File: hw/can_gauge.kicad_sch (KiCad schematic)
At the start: 27 parts, among them J1 Gauge 1, J2 Gauge 2, J3 Gauge 3, J4 Gauge 4, J5 Gauge 5, J6 Power and CAN, U1 PIC16F1459-ISS, U2 MCP2515-xST, U3 MCP2561T-E/SN, U4 74HC595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

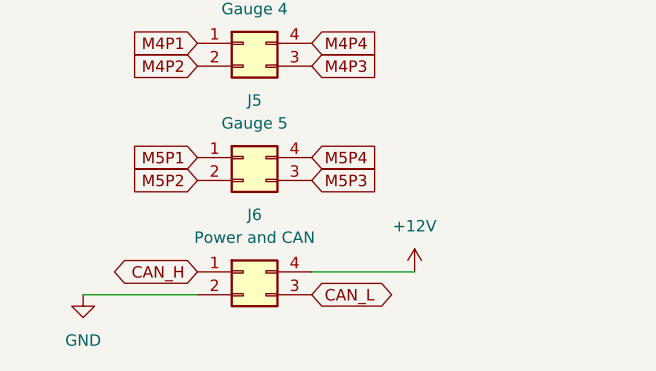
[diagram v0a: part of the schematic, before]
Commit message: hw: change connector layout
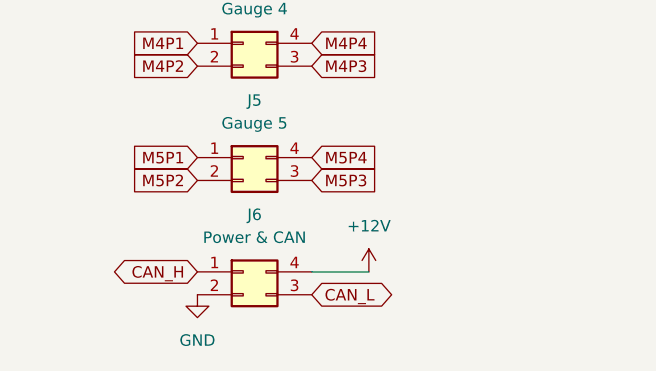
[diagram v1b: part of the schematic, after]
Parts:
- J6: value Power and CAN -> Power & CAN
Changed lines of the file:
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@@
 	(wire
 		(pts
+			(xy 58.42 262.89) (xy 64.77 262.89)
+		)
+		(stroke
+			(width 0)
+			(type default)
+		)
+	)
+	(wire
+		(pts
 			(xy 248.92 123.19) (xy 248.92 186.69)
 		)
@@
 	(wire
 		(pts
-			(xy 58.42 262.89) (xy 69.85 262.89)
-		)
-		(stroke
-			(width 0)
-			(type default)
-		)
-	)
-	(wire
-		(pts
 			(xy 224.79 54.61) (xy 257.81 54.61)
 		)
@@
 	(wire
 		(pts
-			(xy 33.02 265.43) (xy 45.72 265.43)
-		)
-		(stroke
-			(width 0)
-			(type default)
-		)
-	)
-	(wire
-		(pts
 			(xy 341.63 110.49) (xy 344.17 110.49)
 		)
@@
 		(lib_name "GND_5")
 		(lib_id "power:GND")
-		(at 33.02 265.43 0)
+		(at 45.72 265.43 0)
 		(unit 1)
 		(exclude_from_sim no)
@@
 		(fields_autoplaced yes)
 		(property "Reference" "#PWR09"
-			(at 33.02 271.78 0)
+			(at 45.72 271.78 0)
 			(effects
 				(font
@@
 		)
 		(property "Value" "GND"
-			(at 33.02 270.51 0)
+			(at 45.72 270.51 0)
 			(effects
 				(font
@@
 		)
 		(property "Footprint" ""
-			(at 33.02 265.43 0)
+			(at 45.72 265.43 0)
 			(effects
 				(font
@@
 		)
 		(property "Datasheet" ""
-			(at 33.02 265.43 0)
+			(at 45.72 265.43 0)
 			(effects
 				(font
@@
 		)
 		(property "Description" "Power symbol creates a global label with name \"GND\" , ground"
-			(at 33.02 265.43 0)
+			(at 45.72 265.43 0)
 			(effects
 				(font
@@
 		(lib_name "+12V_1")
 		(lib_id "power:+12V")
-		(at 69.85 262.89 0)
+		(at 64.77 262.89 0)
 		(unit 1)
 		(exclude_from_sim no)
@@
 		(fields_autoplaced yes)
 		(property "Reference" "#PWR08"
-			(at 69.85 266.7 0)
+			(at 64.77 266.7 0)
 			(effects
 				(font
@@
 		)
 		(property "Value" "+12V"
-			(at 69.85 257.81 0)
+			(at 64.77 257.81 0)
 			(effects
 				(font
@@
 		)
 		(property "Footprint" ""
-			(at 69.85 262.89 0)
+			(at 64.77 262.89 0)
 			(effects
 				(font
@@
 		)
 		(property "Datasheet" ""
-			(at 69.85 262.89 0)
+			(at 64.77 262.89 0)
 			(effects
 				(font
@@
 		)
 		(property "Description" "Power symbol creates a global label with name \"+12V\""
-			(at 69.85 262.89 0)
+			(at 64.77 262.89 0)
 			(effects
 				(font
@@
 			)
 		)
-		(property "Value" "Power and CAN"
+		(property "Value" "Power & CAN"
 			(at 52.07 259.08 0)
 			(effects

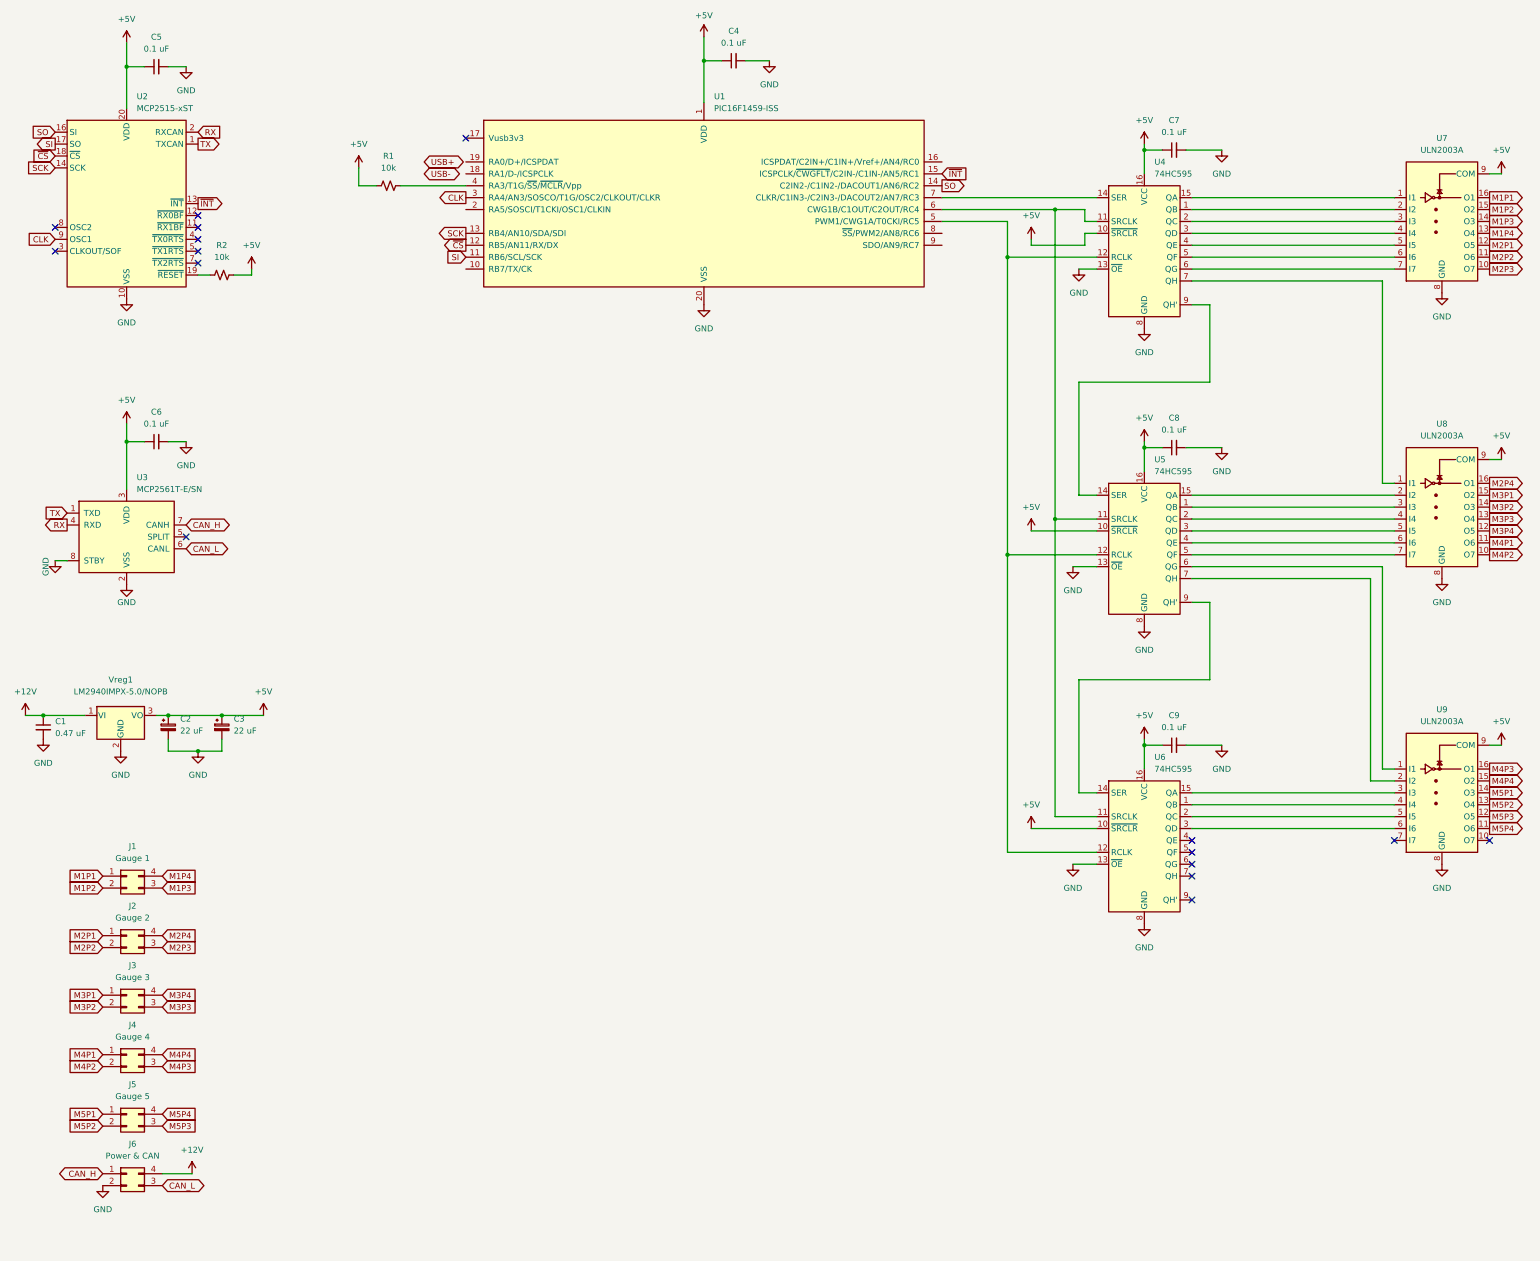
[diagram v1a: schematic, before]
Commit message: hw: 8-way transistor arrays, 6 gauges
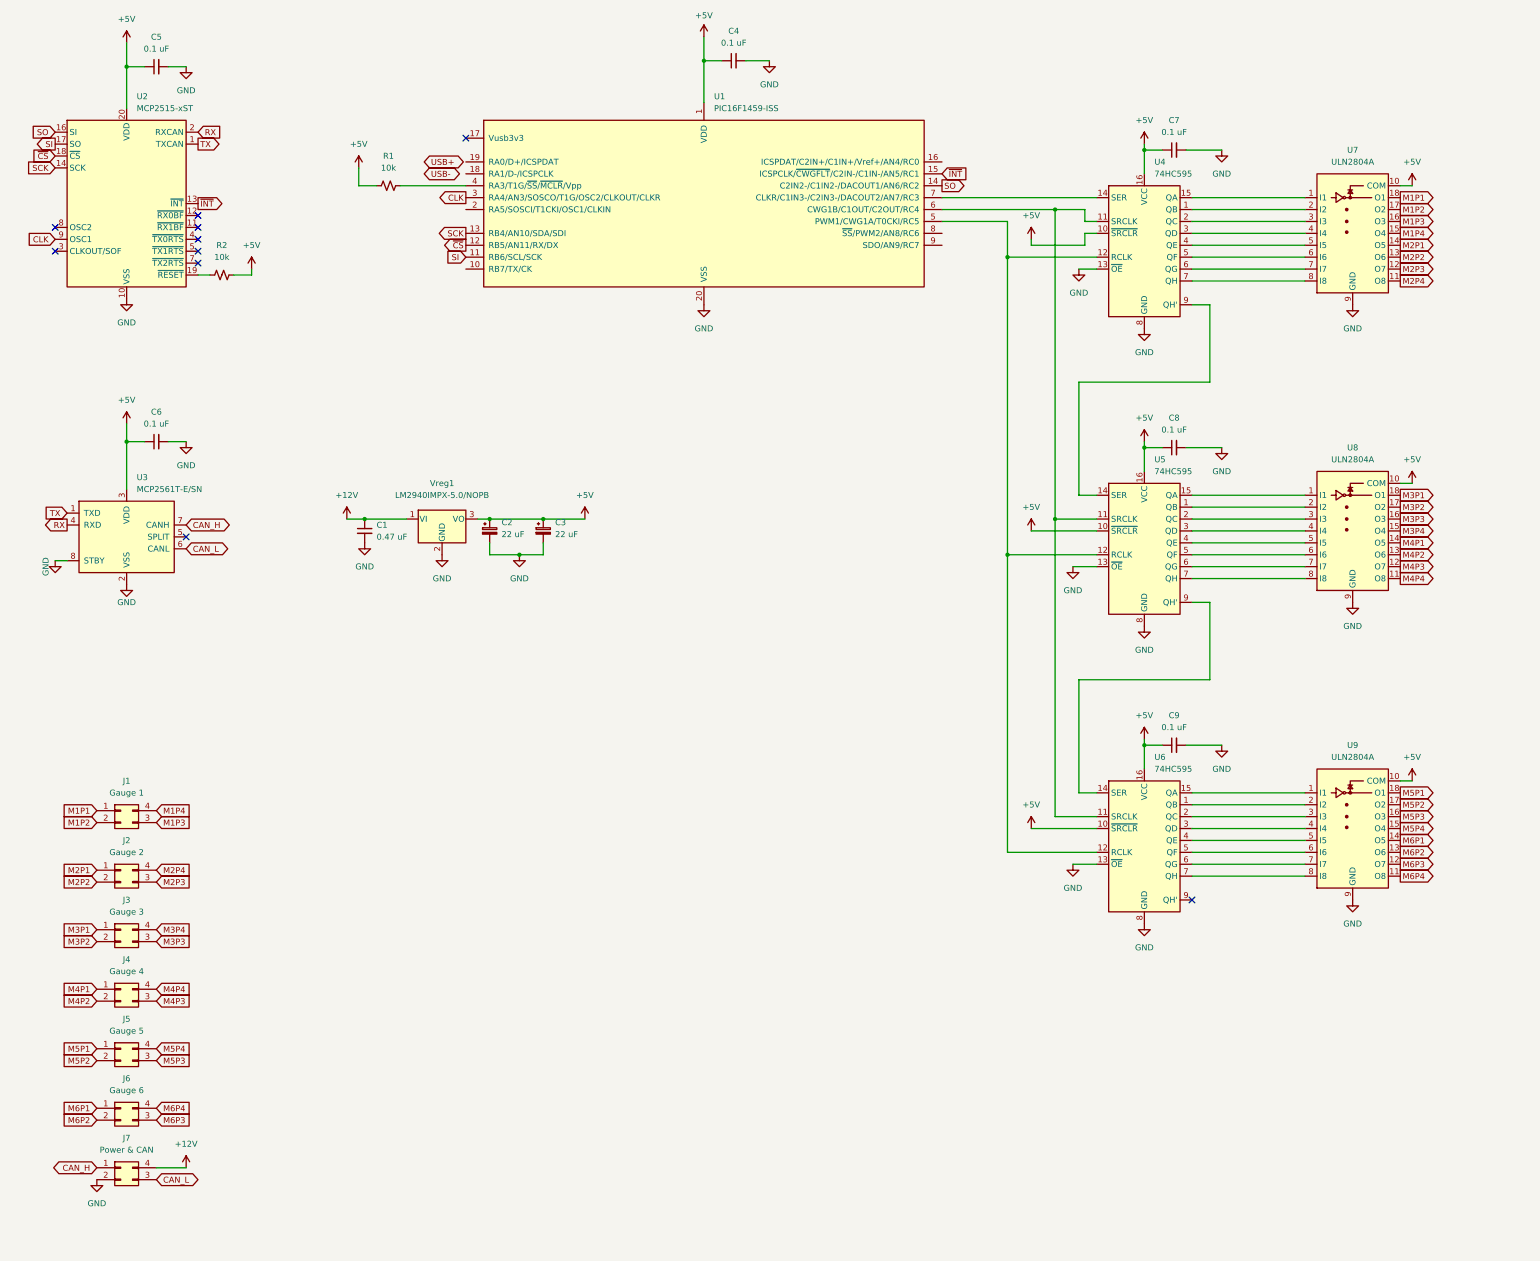
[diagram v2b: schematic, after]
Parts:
- removed U7, U8, U9: ULN2003A, Package_SO:SO-16_3.9x9.9mm_P1.27mm, symbol Transistor_Array:ULN2003A
- added J6: Gauge 6, Connector_Molex:Molex_Mini-Fit_Jr_5569-04A2_2x02_P4.20mm_Horizontal, symbol Connector_Generic:Conn_02x02_Counter_Clockwise
- added U7, U8, U9: ULN2804A, Package_DIP:DIP-18_W7.62mm, symbol Transistor_Array:ULN2804A
- U4, U5, U6: footprint Package_SO:TSSOP-16_4.4x5mm_P0.65mm -> Package_SO:SOIC-16W_7.5x10.3mm_P1.27mm; Digikey (none) -> https://www.digikey.ca/en/products/detail/texas-instruments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
- renumbered J6 to J7
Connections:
- net +5V: now also U7.10 (COM), U8.10 (COM), U9.10 (COM)
- net GND: now also U7.9 (GND), U8.9 (GND), U9.9 (GND)
- net M1P1: now also U7.18 (O1)
- net M1P2: now also U7.17 (O2)
- net M1P3: now also U7.16 (O3)
- net M1P4: now also U7.15 (O4)
- net M2P1: now also U7.14 (O5)
- net M2P2: now also U7.13 (O6)
- net M2P3: now also U7.12 (O7)
- net M2P4: now also U7.11 (O8)
- net M3P1: now also U8.18 (O1)
- net M3P2: now also U8.17 (O2)
- net M3P3: now also U8.16 (O3)
- net M3P4: now also U8.15 (O4)
- net M4P1: now also U8.14 (O5)
- net M4P2: now also U8.13 (O6)
- net M4P3: now also U8.12 (O7)
- net M4P4: now also U8.11 (O8)
- net M5P1: now also U9.18 (O1)
- net M5P2: now also U9.17 (O2)
- net M5P3: now also U9.16 (O3)
- net M5P4: now also U9.15 (O4)
- net at U5.1 (QB): now also U8.2 (I2)
- net at U5.15 (QA): now also U8.1 (I1)
- net at U5.2 (QC): now also U8.3 (I3)
- net at U5.3 (QD): now also U8.4 (I4)
- net at U5.4 (QE): now also U8.5 (I5)
- net at U5.5 (QF): now also U8.6 (I6)
- net at U5.6 (QG): now also U8.7 (I7)
- net at U5.7 (QH): now also U8.8 (I8)
- net at U4.7 (QH): now also U7.8 (I8)
- net at U4.15 (QA): now also U7.1 (I1)
- net at U4.1 (QB): now also U7.2 (I2)
- net at U4.2 (QC): now also U7.3 (I3)
- net at U4.3 (QD): now also U7.4 (I4)
- net at U4.4 (QE): now also U7.5 (I5)
- net at U4.5 (QF): now also U7.6 (I6)
- net at U4.6 (QG): now also U7.7 (I7)
- net at U6.15 (QA): now also U9.1 (I1)
- net at U6.1 (QB): now also U9.2 (I2)
- net at U6.2 (QC): now also U9.3 (I3)
- net at U6.3 (QD): now also U9.4 (I4)
- net at U6.4 (QE): now also U9.5 (I5)
- net at U6.5 (QF): now also U9.6 (I6)
- net at U6.6 (QG): now also U9.7 (I7)
- net at U6.7 (QH): now also U9.8 (I8)
- new net M6P1: J6.1 (Pin_1), U9.14 (O5)
- new net M6P2: J6.2 (Pin_2), U9.13 (O6)
- new net M6P3: J6.3 (Pin_3), U9.12 (O7)
- new net M6P4: J6.4 (Pin_4), U9.11 (O8)
- no-connect marks 16 -> 10
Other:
- moved on the sheet: C1, C2, C3, J1, J2, J3, J4, J5, J7, Vreg1

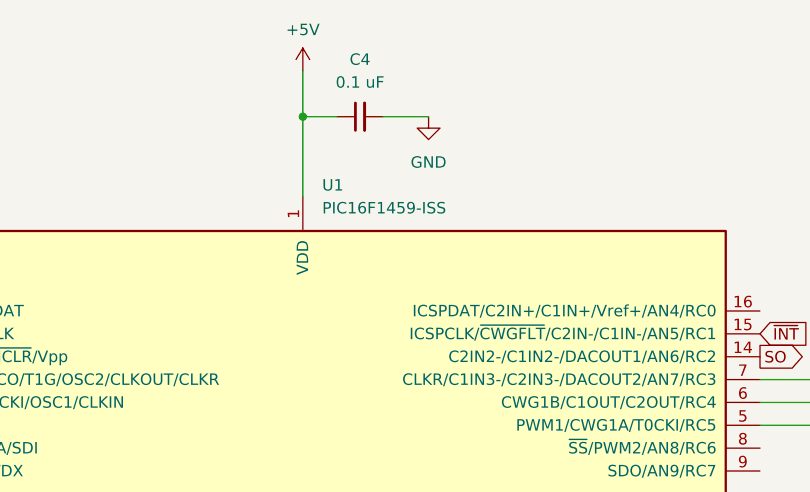
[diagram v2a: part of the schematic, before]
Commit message: hw: through-hole shift registers
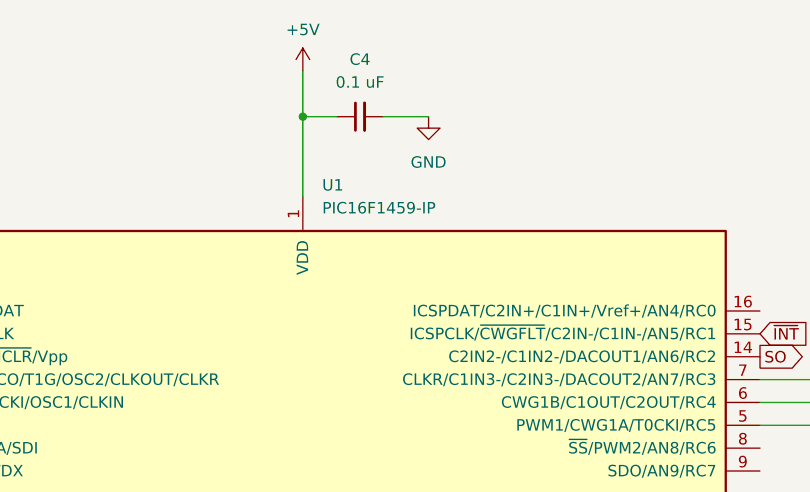
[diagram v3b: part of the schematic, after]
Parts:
- removed U1: PIC16F1459-ISS, Package_SO:SSOP-20_5.3x7.2mm_P0.65mm, symbol MCU_Microchip_PIC16:PIC16F1459-ISS
- added U1: PIC16F1459-IP, Package_DIP:DIP-20_W7.62mm, symbol MCU_Microchip_PIC16:PIC16F1459-IP
- C4, C5, C6, C7, C8, C9: footprint Capacitor_SMD:C_0402_1005Metric -> Capacitor_THT:C_Rect_L4.0mm_W2.5mm_P2.50mm; Digikey https://www.digikey.ca/en/products/detail/murata-electronic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 -> https://www.digikey.ca/en/products/detail/tdk-corporation/F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
- U4, U5, U6: footprint Package_SO:SOIC-16W_7.5x10.3mm_P1.27mm -> Package_DIP:DIP-16_W7.62mm; Digikey https://www.digikey.ca/en/products/detail/texas-instruments/SN74HC595DR/562919 -> https://www.digikey.ca/en/products/detail/texas-instruments/SN74HC595N/277246?s=N4IgjCBcpgTAnBaIDGUBmBDANgZwKYA0IA9lANrgAMAHACx2wgC6xADgC5QgDKHATgEsAdgHMQAX2Jh4NeFFBpIWPEVIUQVFlJABaJsiUCArmrKRKAVm3Fd8w1BNmNEZhJ0HKuYQHY6ACxRLeGtWEAA2BRBBABNuXTAqCHYuSBAQYg4ATzZ8bkxcNHcgA
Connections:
- net +5V: now also U1.1 (VDD)
- net CLK: now also U1.3 (RA4/AN3/SOSCO/T1G/OSC2/CLKOUT/CLKR)
- net GND: now also U1.20 (VSS)
- net SCK: now also U1.13 (RB4/AN10/SDA/SDI)
- net SI: now also U1.11 (RB6/SCL/SCK)
- net SO: now also U1.14 (C2IN2-/C1IN2-/DACOUT1/AN6/RC2)
- net ~{CS}: now also U1.12 (RB5/AN11/RX/DX)
- net ~{INT}: now also U1.15 (ICSPCLK/~{CWGFLT}/C2IN-/C1IN-/AN5/RC1)
- net at R1.2: now also U1.4 (RA3/T1G/~{SS}/~{MCLR}/Vpp)
- net at U4.12 (RCLK), U5.12 (RCLK), U6.12 (RCLK): now also U1.5 (PWM1/CWG1A/T0CKI/RC5)
- net at U4.11 (SRCLK), U5.11 (SRCLK), U6.11 (SRCLK): now also U1.6 (CWG1B/C1OUT/C2OUT/RC4)
- net at U4.14 (SER): now also U1.7 (CLKR/C1IN3-/C2IN3-/DACOUT2/AN7/RC3)
